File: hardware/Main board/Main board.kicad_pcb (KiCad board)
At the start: 2 copper layers, 105 parts, among them J1 Wind Direction, J10 Free Pins, J11 Nokia 5110 LCD, J2 Wind Speed, J3 USB_B_Micro, J4 Micro_SD_Card, J5 Sensor board connector, J6 Barrel_Jack, J7 ISP programmer, J8 SPI1, J9 SPI2, Q1 IRLML2060, SW1 SW_Push, SW2 SW_SPST, SW3 SW_Push, SW4 SW_Push, SW5 Page Switch btn, U1 FT232RL, U2 MCP6042, U3 SCWN03A-03, U4 ATmega1284P-AU, U5 DS3231MZ, U6 ENC28J60, U7 USB6B1, U8 DRV5053, Y1 16MHZ

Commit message: Minor update to the main board
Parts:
- added REF**: Polarity_Center_Positive_6mm_SilkScreen, Symbol:Polarity_Center_Positive_6mm_SilkScreen, F.Cu at (48.0, 92.5)
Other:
- board outline added: 236.5 x 92.5 mm
- board text added: "Motherboard for a weather station v1 by Daniels Fišers 26/07/2019"
- board text removed: "Motherboard for a weather station v0.5 by Daniels Fišers"

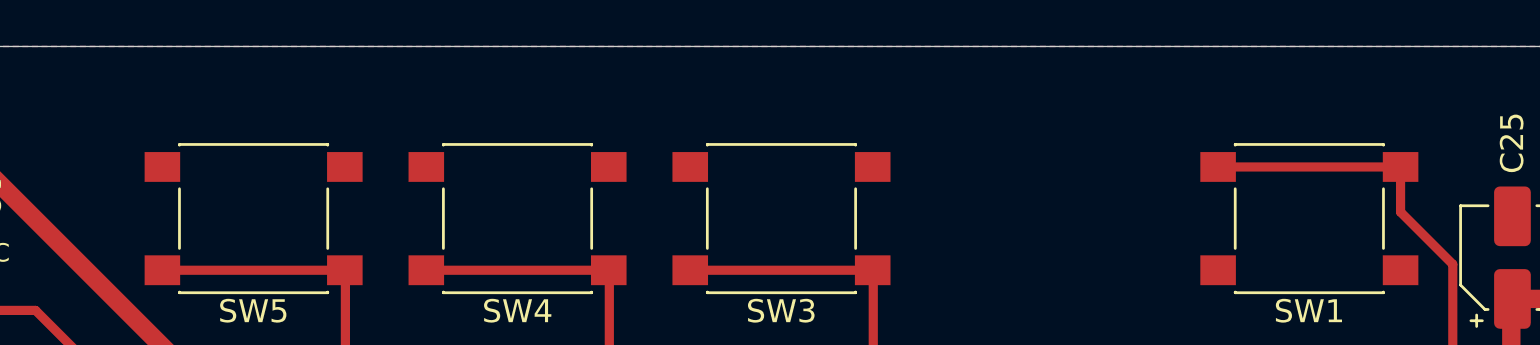
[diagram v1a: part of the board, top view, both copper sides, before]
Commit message: Added button labels
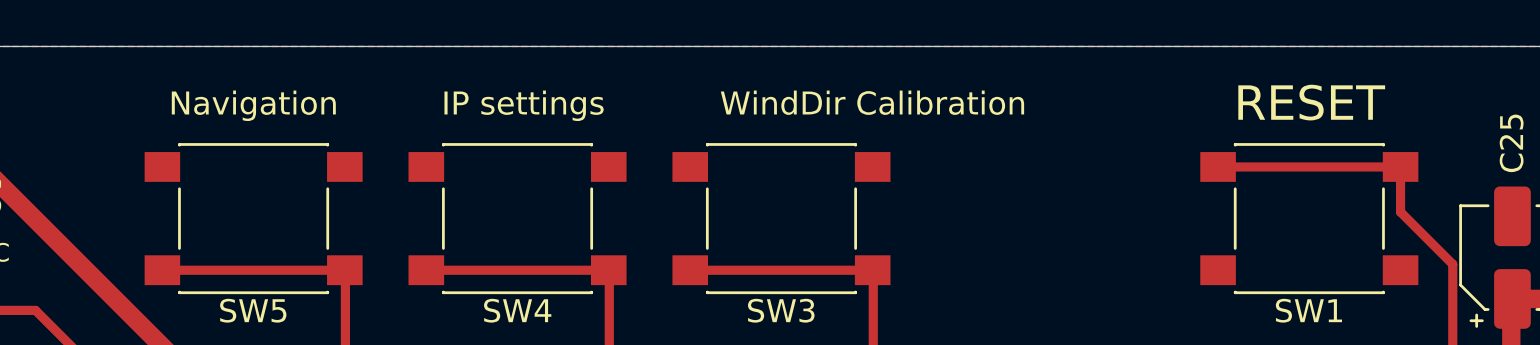
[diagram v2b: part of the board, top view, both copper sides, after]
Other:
- board text added: "IP settings"
- board text added: "Navigation"
- board text added: "RESET"
- board text added: "WindDir Calibration"
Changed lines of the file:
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@@
   (general
     (thickness 1.6)
-    (drawings 77)
+    (drawings 81)
     (tracks 714)
     (zones 0)
@@
     )
   )
+  (gr_text Navigation (at 156.75 32.5) (layer F.SilkS)
+    (effects (font (size 1 1) (thickness 0.15)))
+  )
+  (gr_text "IP settings" (at 168.5 32.5) (layer F.SilkS)
+    (effects (font (size 1 1) (thickness 0.15)))
+  )
+  (gr_text "WindDir Calibration" (at 183.75 32.5) (layer F.SilkS)
+    (effects (font (size 1 1) (thickness 0.15)))
+  )
+  (gr_text RESET (at 202.75 32.5) (layer F.SilkS)
+    (effects (font (size 1.5 1.5) (thickness 0.15)))
+  )
   (gr_text 12V (at 57 103) (layer F.SilkS)

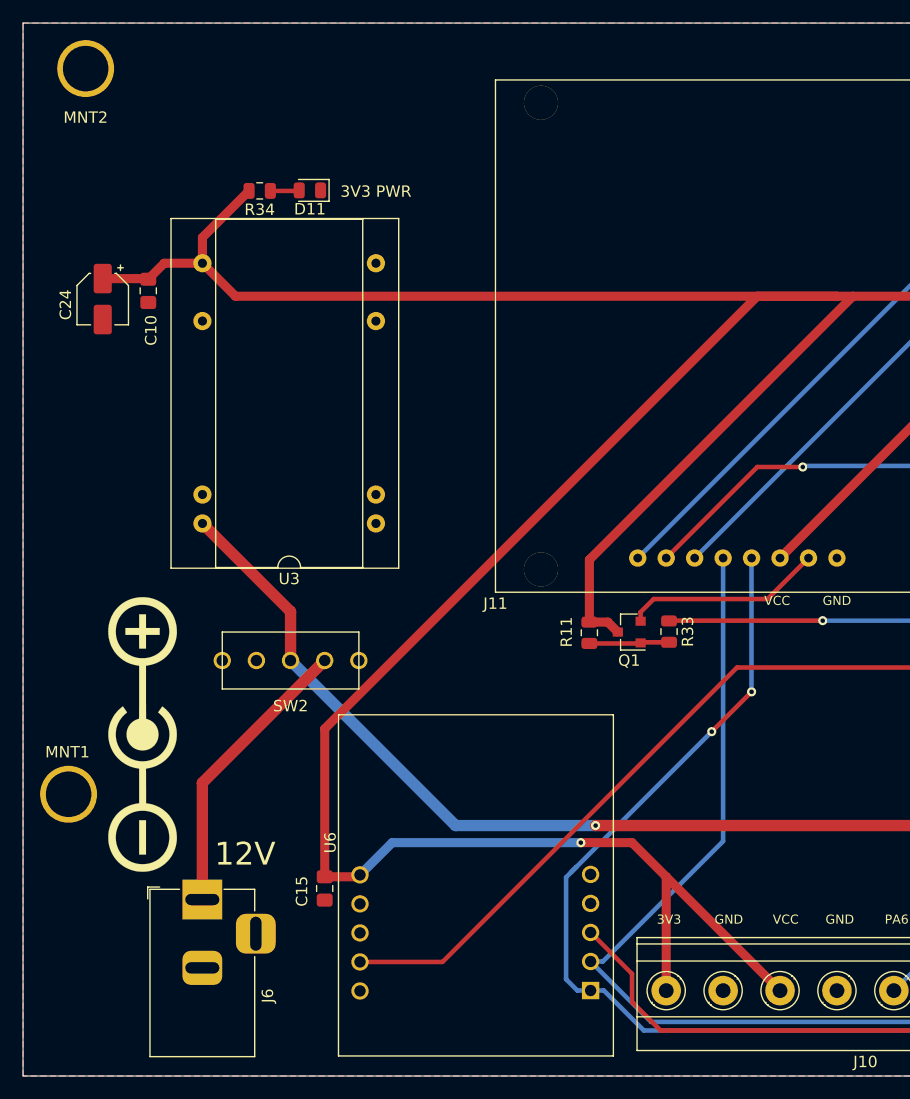
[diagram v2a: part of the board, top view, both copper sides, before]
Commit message: Added protection for power input
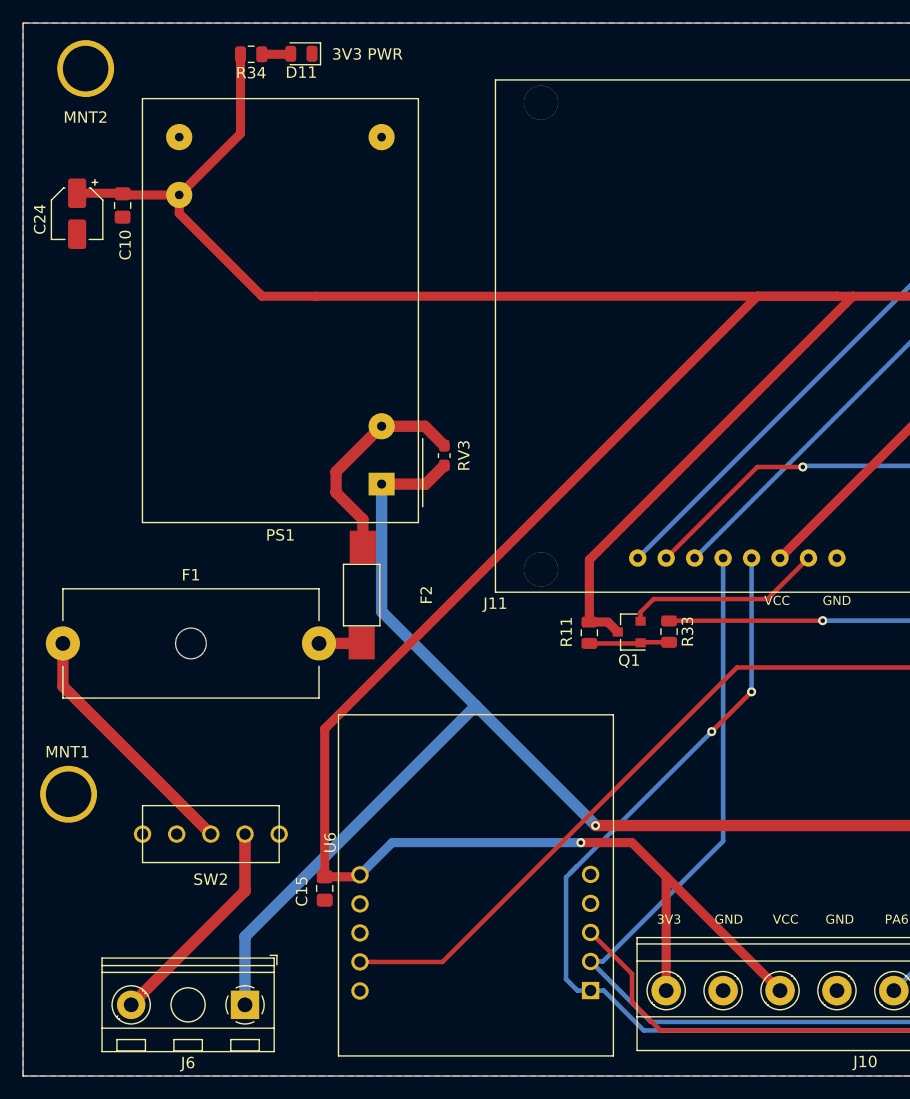
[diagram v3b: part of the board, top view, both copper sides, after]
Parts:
- removed REF**: Polarity_Center_Positive_6mm_SilkScreen, Symbol:Polarity_Center_Positive_6mm_SilkScreen
- removed U3: SCWN03A-03, Meteo_Footprints:SCWN03A
- added F1: Fuse 100mA, Fuse:Fuseholder_Cylinder-5x20mm_Schurter_0031_8201_Horizontal_Open, F.Cu at (41.0, 84.5)
- added F2: Fuse 72C, Meteo_Footprints:Thermal fuse, F.Cu at (67.2, 80.2)
- added PS1: IRM-03-3.3, Converter_ACDC:Converter_ACDC_MeanWell_IRM-03-xx_THT, F.Cu at (69.0, 70.5)
- added RV3: Varistor, Capacitor_SMD:C_0603_1608Metric_Pad1.05x0.95mm_HandSolder, F.Cu at (74.5, 68.0)
- J6: value Barrel_Jack -> Screw_Terminal_01x02; footprint Connector_BarrelJack:BarrelJack_Horizontal -> TerminalBlock_RND:TerminalBlock_RND_205-00298_1x02_P10.00mm_Horizontal
- moved SW2 16.8 mm to (54.0, 101.2)
- moved D11 12.0 mm to (62.0, 32.7)
- moved R34 12.0 mm to (57.5, 32.7)
- moved J6 9.98 mm to (57.0, 116.2), turned to 180 degrees
- moved C10 7.83 mm to (46.2, 46.0)
- moved C24 7.83 mm to (42.2, 46.8)
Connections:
- J6 pad 2: GND -> 230V
- JP1 pad 3: 12V -> 230V
- SW2 pad 2: 12V -> Net-(F1-Pad1)
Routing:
- net 230V: track 0.00 -> 189.3 mm, vias 0 -> 2
- net 12V: track 158.7 -> 0.00 mm, vias 2 -> 0
- net Net-(F1-Pad1): track 0.00 -> 22.1 mm
- net Net-(F2-Pad2): track 0.00 -> 19.5 mm
- net VCC: track 804.0 -> 815.6 mm
- net Net-(J6-Pad1): track 25.5 -> 19.1 mm
- net Net-(F1-Pad2): track 0.00 -> 3.77 mm

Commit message: Updated the power supply input
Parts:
- removed F2: Fuse 72C, Meteo_Footprints:Thermal fuse
- removed JP1: Jumper 3v3/12v, Connector_PinHeader_2.54mm:PinHeader_1x03_P2.54mm_Vertical
- added C26: 4.7uF, Capacitor_SMD:CP_Elec_4x5.4, F.Cu at (36.2, 46.8)
- added J12: 3v3 in, TerminalBlock:TerminalBlock_Altech_AK300-2_P5.00mm, F.Cu at (37.2, 114.5)
- added REF**: Symbol_Highvoltage_Type1_CopperTop_Small, Symbol:Symbol_Highvoltage_Type1_CopperTop_Small, F.Cu at (59.8, 109.2)
- J6: value Screw_Terminal_01x02 -> 230V AC IN
- SW2: footprint Meteo footprint:Switch_ON_OFF -> Meteo_Footprints:Switch_NEW
- moved D11 32.3 mm to (45.8, 60.7), turned to 90 degrees
- moved R34 26.3 mm to (45.8, 56.3), turned to 90 degrees
- moved MNT1 4.25 mm to (37.2, 97.8)
- moved MNT2 4.25 mm to (38.8, 34.0)
- moved MNT3 4.25 mm to (263.8, 34.0)
- moved MNT4 4.25 mm to (265.2, 97.8)
- moved J6 3.51 mm to (60.5, 116.5)
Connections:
- net 230V renamed Net-(J6-Pad2)
- PS1 pad 3: Net-(F2-Pad2) -> Net-(F1-Pad2)
- R2 pad 1: Net-(JP1-Pad2) -> VCC
- RV3 pad 2: Net-(F2-Pad2) -> Net-(F1-Pad2)
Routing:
- net Net-(J6-Pad2): track 189.3 -> 55.7 mm, vias 2 -> 0
- net VCC: track 815.6 -> 909.6 mm, vias 4 -> 5
- net Net-(F1-Pad2): track 3.77 -> 27.6 mm
- net Net-(F2-Pad2): track 19.5 -> 0.00 mm
- net Net-(JP1-Pad2): track 3.75 -> 0.00 mm
- net Net-(J6-Pad1): track 19.1 -> 18.2 mm
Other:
- board size 236.5 x 92.5 mm -> 237.8 x 92.5 mm
- board text added: "230V"
- board text removed: "12V"

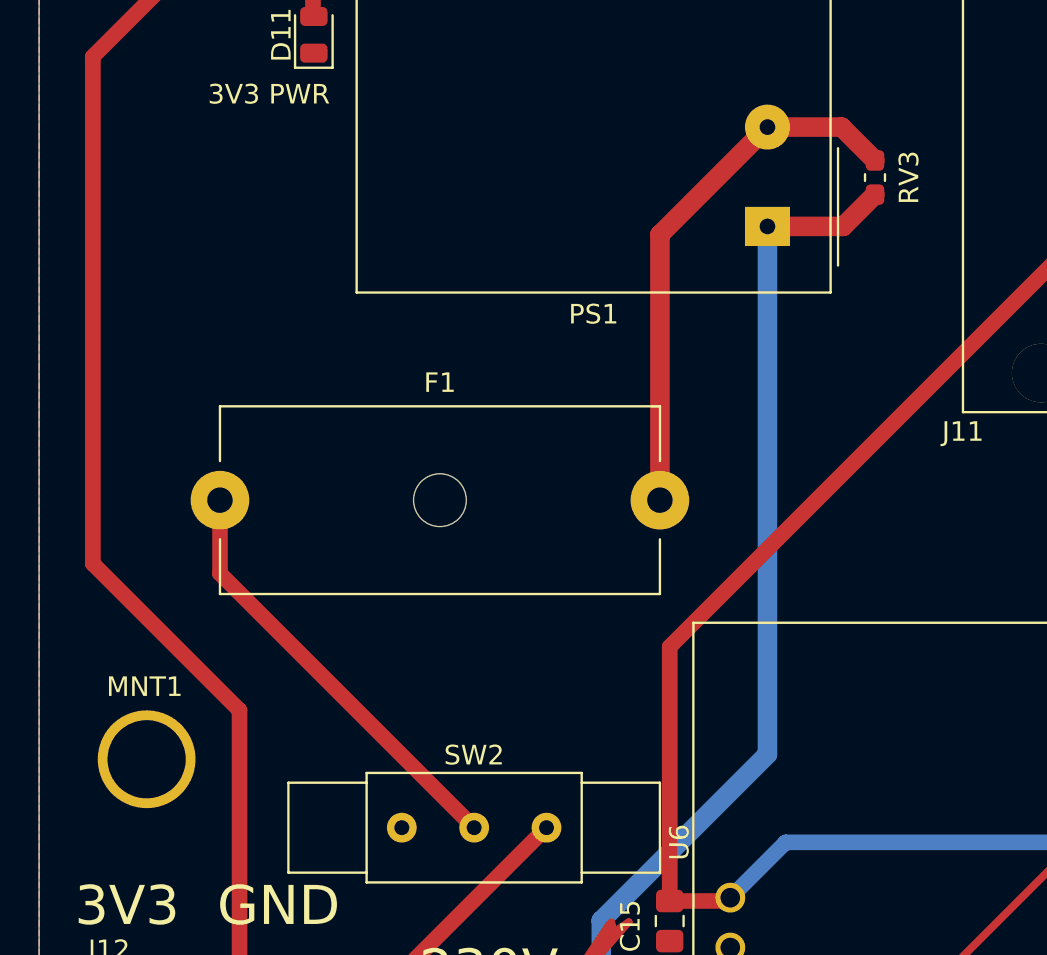
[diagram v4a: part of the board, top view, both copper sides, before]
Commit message: Changed varistor footprint
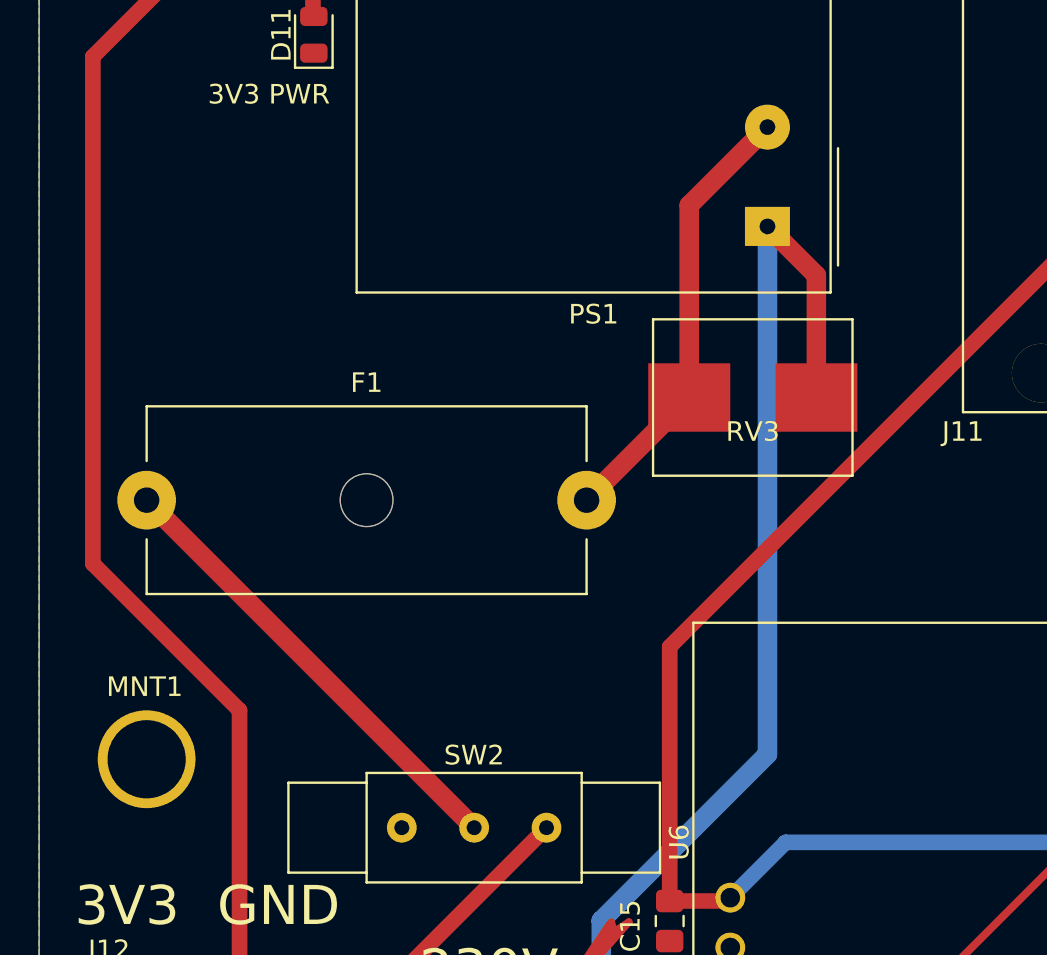
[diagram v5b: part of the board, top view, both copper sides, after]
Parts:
- RV3: footprint Capacitor_SMD:C_0603_1608Metric_Pad1.05x0.95mm_HandSolder -> Meteo_Footprints:Varistor_SMD
- moved RV3 12.9 mm to (68.2, 79.2), turned to 0 degrees
- moved F1 3.75 mm to (37.2, 84.5)
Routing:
- net Net-(F1-Pad2): track 27.6 -> 22.9 mm
- net Net-(J6-Pad2): track 55.7 -> 59.3 mm
- net Net-(F1-Pad1): track 22.1 -> 23.7 mm
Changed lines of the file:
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@@
     (thickness 1.6)
     (drawings 81)
-    (tracks 729)
+    (tracks 727)
     (zones 0)
     (modules 109)
@@
     (add_net speedOUT)
   )
+  (module Meteo_Footprints:Varistor_SMD (layer F.Cu)
+    (at 68.25 79.25)
+    (fp_text reference RV3 (at 0 1.75) (layer F.SilkS)
+      (effects (font (size 1 1) (thickness 0.15)))
+    )
+    (fp_text value Varistor (at 0 1.43) (layer F.Fab)
+      (effects (font (size 1 1) (thickness 0.15)))
+    )
+    (fp_line (start -5.1 4) (end 5.1 4) (layer F.SilkS) (width 0.12))
+    (fp_line (start -5.1 -4) (end -5.1 4) (layer F.SilkS) (width 0.12))
+    (fp_line (start 5.1 -4) (end 5.1 4) (layer F.SilkS) (width 0.12))
+    (fp_line (start -5.1 -4) (end 5.1 -4) (layer F.SilkS) (width 0.12))
+    (fp_text user %R (at 0 0 90) (layer F.Fab)
+      (effects (font (size 0.4 0.4) (thickness 0.06)))
+    )
+    (pad 2 smd rect (at -3.25 0 90) (size 3.5 4.2) (layers F.Cu F.Paste F.Mask)
+      (net 99 "Net-(F1-Pad2)"))
+    (pad 1 smd rect (at 3.25 0 90) (size 3.5 4.2) (layers F.Cu F.Paste F.Mask)
+      (net 101 "Net-(J6-Pad2)"))
+  )
   (module Symbol:Symbol_Highvoltage_Type1_CopperTop_Small (layer F.Cu)
     (at 59.75 109.25)
@@
     )
   )
-  (module Capacitor_SMD:C_0603_1608Metric_Pad1.05x0.95mm_HandSolder (layer F.Cu)
-    (at 74.5 68 90)
-    (descr "Capacitor SMD 0603 (1608 Metric), square (rectangular) end terminal, IPC_7351 nominal with elongated pad for handsoldering. (Body size source: http://www.tortai-tech.com/upload/download/2011102023233369053.pdf), generated with kicad-footprint-generator")
-    (tags "capacitor handsolder")
-    (attr smd)
-    (fp_text reference RV3 (at 0 1.75 90) (layer F.SilkS)
-      (effects (font (size 1 1) (thickness 0.15)))
-    )
-    (fp_text value Varistor (at 0 1.43 90) (layer F.Fab)
-      (effects (font (size 1 1) (thickness 0.15)))
-    )
-    (fp_text user %R (at 0 0 90) (layer F.Fab)
-      (effects (font (size 0.4 0.4) (thickness 0.06)))
-    )
-    (fp_line (start 1.65 0.73) (end -1.65 0.73) (layer F.CrtYd) (width 0.05))
-    (fp_line (start 1.65 -0.73) (end 1.65 0.73) (layer F.CrtYd) (width 0.05))
-    (fp_line (start -1.65 -0.73) (end 1.65 -0.73) (layer F.CrtYd) (width 0.05))
-    (fp_line (start -1.65 0.73) (end -1.65 -0.73) (layer F.CrtYd) (width 0.05))
-    (fp_line (start -0.171267 0.51) (end 0.171267 0.51) (layer F.SilkS) (width 0.12))
-    (fp_line (start -0.171267 -0.51) (end 0.171267 -0.51) (layer F.SilkS) (width 0.12))
-    (fp_line (start 0.8 0.4) (end -0.8 0.4) (layer F.Fab) (width 0.1))
-    (fp_line (start 0.8 -0.4) (end 0.8 0.4) (layer F.Fab) (width 0.1))
-    (fp_line (start -0.8 -0.4) (end 0.8 -0.4) (layer F.Fab) (width 0.1))
-    (fp_line (start -0.8 0.4) (end -0.8 -0.4) (layer F.Fab) (width 0.1))
-    (pad 2 smd roundrect (at 0.875 0 90) (size 1.05 0.95) (layers F.Cu F.Paste F.Mask) (roundrect_rratio 0.25)
-      (net 99 "Net-(F1-Pad2)"))
-    (pad 1 smd roundrect (at -0.875 0 90) (size 1.05 0.95) (layers F.Cu F.Paste F.Mask) (roundrect_rratio 0.25)
-      (net 101 "Net-(J6-Pad2)"))
-    (model ${KISYS3DMOD}/Capacitor_SMD.3dshapes/C_0603_1608Metric.wrl
-      (at (xyz 0 0 0))
-      (scale (xyz 1 1 1))
-      (rotate (xyz 0 0 0))
-    )
-  )
   (module Fuse:Fuseholder_Cylinder-5x20mm_Schurter_0031_8201_Horizontal_Open (layer F.Cu)
-    (at 41 84.5)
+    (at 37.25 84.5)
     (descr "Fuseholder horizontal open 5x20 Schurter 0031.8201, https://www.schurter.com/en/datasheet/typ_OGN.pdf")
     (tags "Fuseholder horizontal open 5x20 Schurter 0031.8201")
@@
   (segment (start 45.755 59.7175) (end 45.8 59.7625) (width 0.8) (layer F.Cu) (net 98))
   (segment (start 45.755 57.2275) (end 45.755 59.7175) (width 0.8) (layer F.Cu) (net 98))
-  (segment (start 72.795 65.42) (end 74.5 67.125) (width 1) (layer F.Cu) (net 99))
-  (segment (start 69 65.42) (end 72.795 65.42) (width 1) (layer F.Cu) (net 99))
-  (segment (start 63.5 70.92) (end 69 65.42) (width 1) (layer F.Cu) (net 99))
-  (segment (start 63.5 84.5) (end 63.5 70.92) (width 1) (layer F.Cu) (net 99))
-  (segment (start 41 88.25) (end 41 84.5) (width 0.8) (layer F.Cu) (net 100))
-  (segment (start 54 101.25) (end 41 88.25) (width 0.8) (layer F.Cu) (net 100))
-  (segment (start 72.875 70.5) (end 74.5 68.875) (width 1) (layer F.Cu) (net 101))
-  (segment (start 69 70.5) (end 72.875 70.5) (width 1) (layer F.Cu) (net 101))
+  (segment (start 59.75 84.5) (end 65 79.25) (width 1) (layer F.Cu) (net 99))
+  (segment (start 65 69.42) (end 69 65.42) (width 1) (layer F.Cu) (net 99))
+  (segment (start 65 79.25) (end 65 69.42) (width 1) (layer F.Cu) (net 99))
+  (segment (start 54 101.25) (end 37.25 84.5) (width 1) (layer F.Cu) (net 100))
   (segment (start 60.5 116.5) (end 60.5 106) (width 1) (layer B.Cu) (net 101))
   (segment (start 69 97.5) (end 69 70.5) (width 1) (layer B.Cu) (net 101))
   (segment (start 60.5 106) (end 69 97.5) (width 1) (layer B.Cu) (net 101))
+  (segment (start 71.5 73) (end 69 70.5) (width 1) (layer F.Cu) (net 101))
+  (segment (start 71.5 79.25) (end 71.5 73) (width 1) (layer F.Cu) (net 101))
   (zone (net 2) (net_name GND) (layer F.Cu) (hatch edge 0.508)
     (connect_pads (clearance 0.2))
     (min_thickness 0.2)
-    (fill yes (arc_segments 32) (thermal_gap 0.2) (thermal_bridge_width 0.508))
+    (fill (arc_segments 32) (thermal_gap 0.2) (thermal_bridge_width 0.508))
     (polygon
       (pts
@@
     (connect_pads (clearance 0.2))
     (min_thickness 0.2)
-    (fill yes (arc_segments 32) (thermal_gap 0.2) (thermal_bridge_width 0.508))
+    (fill (arc_segments 32) (thermal_gap 0.2) (thermal_bridge_width 0.508))
     (polygon
       (pts
